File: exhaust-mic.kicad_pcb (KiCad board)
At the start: 4 copper layers, 72 x 55 mm, 131 parts, among them J1 XH-6pol_Power_CAN, J2 XH-5pol_MicA, J3 XH-5pol_MicB, J4 USB-C, J5 microSD_PushPush, J6 GPS_unbestueckt, J7 I2C_Erweiterung, Q1 ZXMP6A17E6, Q3 2N7002, Q4 2N7002, SW1 RESET, SW2 BOOT, SW3 REC, SW4 MARK, U1 LM5164DDA, U2 TLV1117LV33, U3 TPS7A2033, U5 PCM1863DBT, U6 ESP32-S3-WROOM-1-N8R2, U7 DS3231SN, U8 SN65HVD230D, Y1 24.576MHz

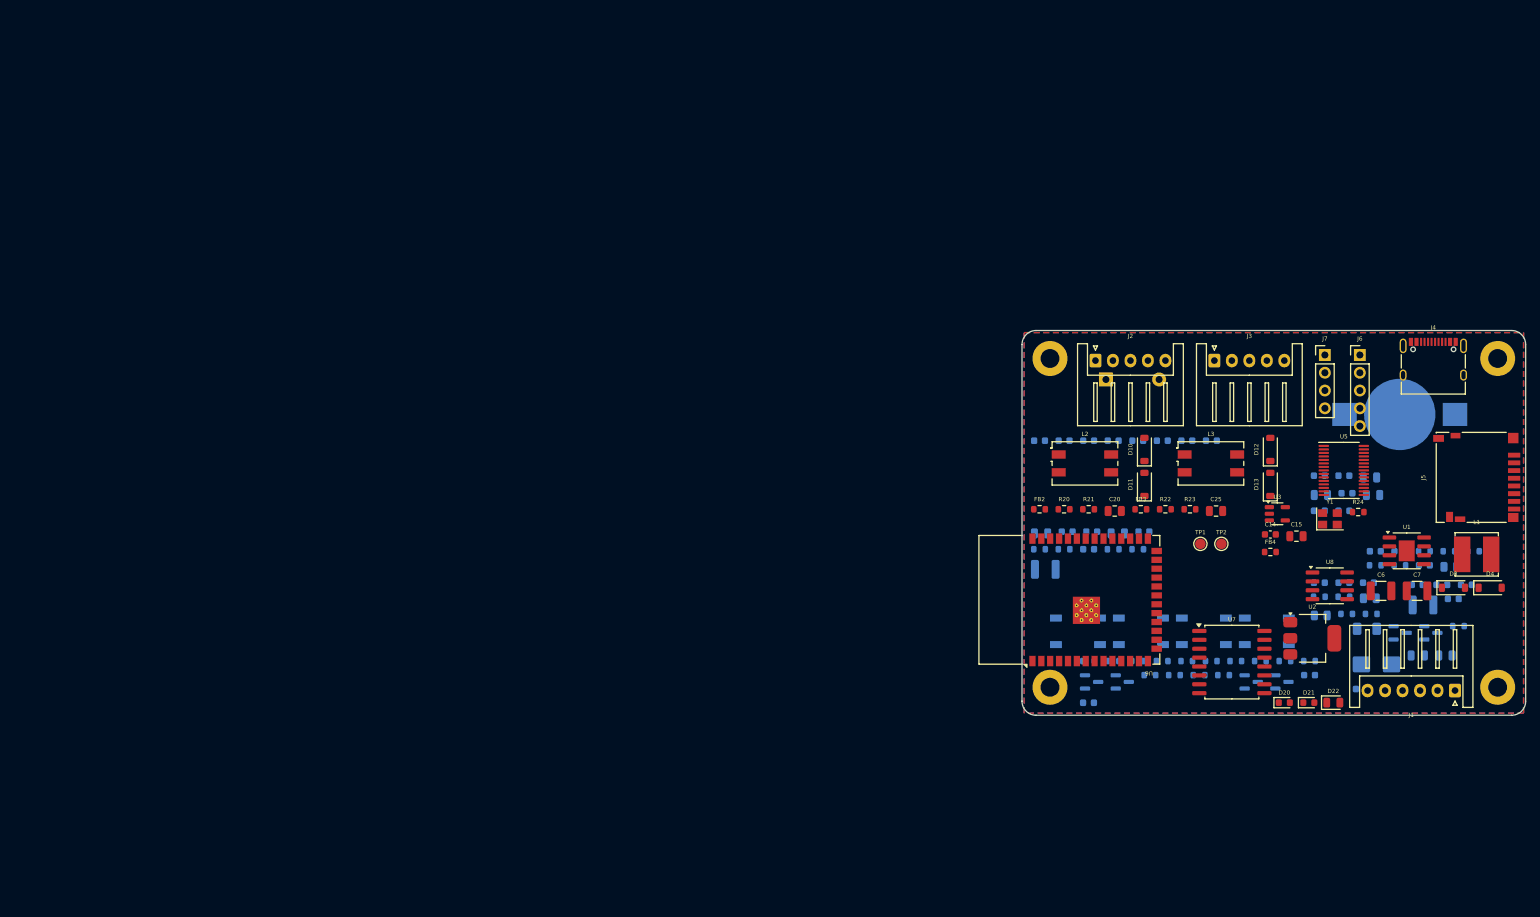
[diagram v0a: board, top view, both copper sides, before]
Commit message: Layout verdrahten, ERC/DRC bereinigen, Werkzeugkette auf KiCad 10
Mikrofonkopf ist fertig verdrahtet (0 offene Verbindungen, 0 DRC-Fehler).
Auf der Hauptplatine bleiben 16 Verbindungen offen, ebenfalls ohne
DRC-Fehler; sie sind im interaktiven Router von KiCad zu schliessen.

Schaltplan
- 3 Speisepin-Fehler behoben (+4V6, ADC-AVDD, Uhrenbatterie brauchen ein
  Speiseflag - sie werden ueber Drossel, Ferrit bzw. Zelle gespeist und
  haben damit keine Quelle im Sinne der Regelpruefung)
- Netzname GND_CHASSIS entfernt: lag auf demselben Knoten wie GND
- TLV1117LV33 hatte einen Pin 4 fuer die Kuehlfahne, den es im Footprint
  SOT-223-3_TabPin2 nicht gibt - dort traegt Pad 2 die Fahne
- Piezo von Durchsteck- auf SMD-Ausfuehrung (Murata PKMCS0909E): fuer den
  12,5-mm-Typ gibt es keine Position, an der seine Anschluesse nicht auf
  der Gegenseite auf Pads treffen
- ERC laeuft jetzt fehlerfrei

Layout
- Durchsteckpads belegen beide Seiten. J1, J4 und J6 standen ueber
  rueckseitigen Bauteilen; das waren vier echte Kurzschluesse, unter
  anderem GPS_PPS gegen Masse an der Knopfzelle. Die eigene Pruefung
  vergleicht Durchsteckpads jetzt gegen beide Seiten, pad-genau
- In2 traegt keine Versorgungsinseln mehr, sondern Signale. Vorher wich
  der Autorouter auf die Masseflaeche aus - 140 Segmente aus 30 Netzen
  quer durch In1. Der DSN-Export kennzeichnet In1 nun als Versorgungslage
- Masseflaechen auf den Aussenlagen mit Naehvias an In1 angebunden und auf
  automatische Inselentfernung gestellt
- Netzklasse auf 0,18 mm Bahn, 0,15 mm Abstand, 0,5/0,25-mm-Via verengt;
  mit KiCads Vorgabewerten blieb rund ein Dutzend Verbindungen mehr offen
- Beschaffungsfelder unsichtbar und auf die Fab-Lage: sichtbar im
  Siebdruck ueberdecken die Herstellernummern die halbe Platine, das
  waren 151 der urspruenglich 214 Regelwarnungen

Werkzeuge
- pipeline.sh fasst den Layoutlauf zusammen
- fix_drc.py nimmt KiCads Regelpruefung als Instanz und entfernt, was sie
  beanstandet - die eigenen Abst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
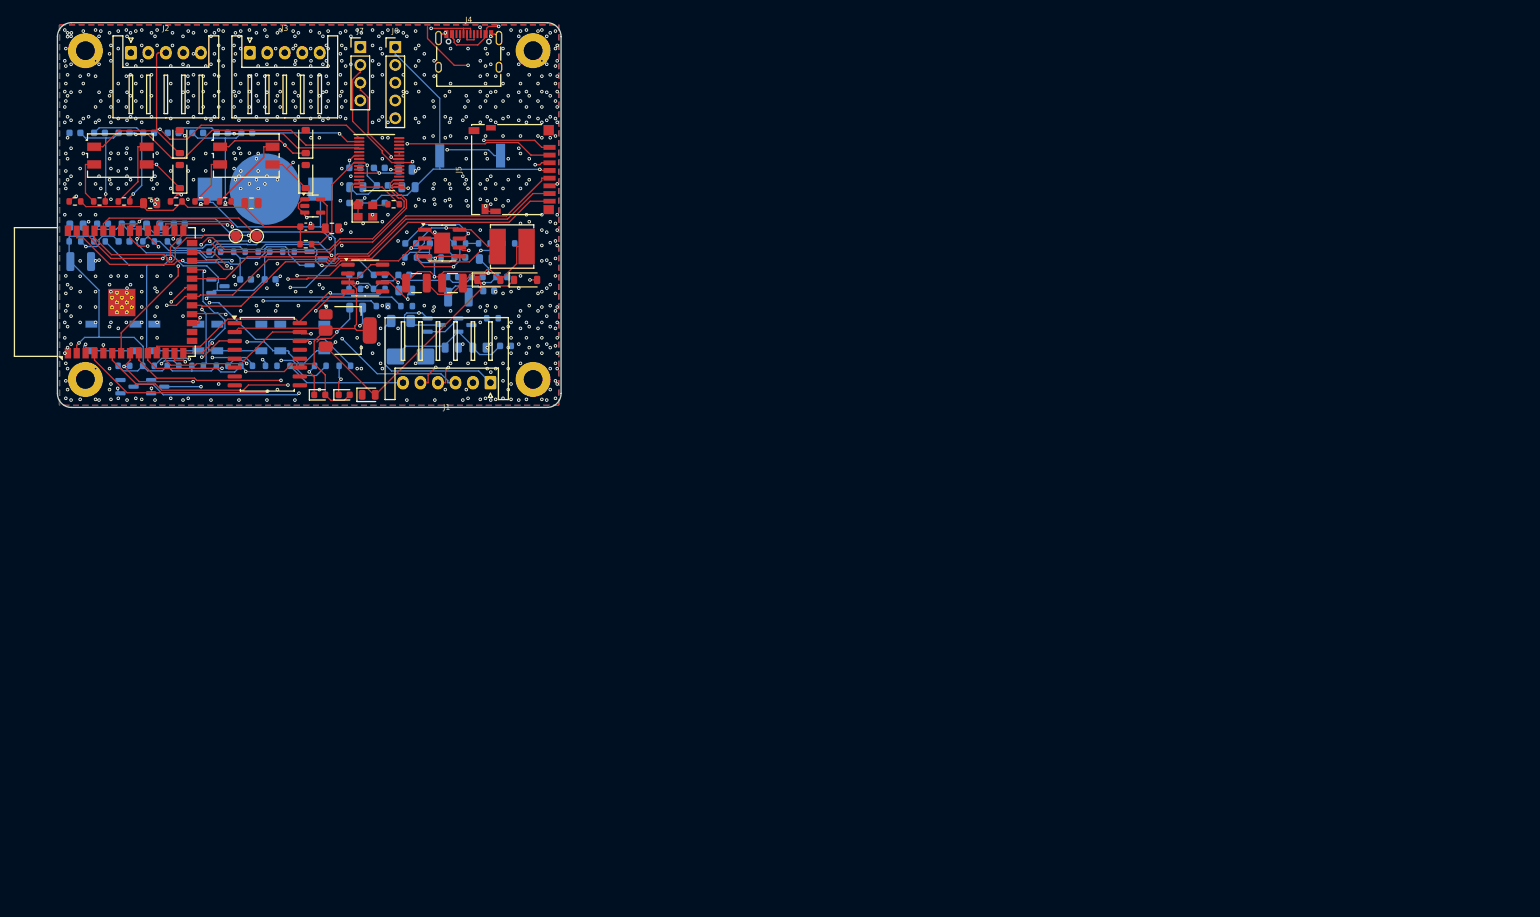
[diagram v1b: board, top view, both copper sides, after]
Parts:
- BT1: footprint BatteryHolder_Keystone_3000_1x12mm -> Battery:BatteryHolder_Keystone_3000_1x12mm
- C1, C15, C2, C20, C25, C32, C33, C35, C41, C45: footprint C_0805_2012Metric -> Capacitor_SMD:C_0805_2012Metric
- C10, C12, C13, C14, C16, C17, C21, C22, C23, C24, C26, C27, C28, C29, C3, C30, C31, C34, C36, C37, C4, C42, C43, C44, C46, C5, C50, C51, C52, C8, C9: footprint C_0603_1608Metric -> Capacitor_SMD:C_0603_1608Metric
- C11, C40, C6, C7: footprint C_1210_3225Metric -> Capacitor_SMD:C_1210_3225Metric
- D1, D5, D6, Q1, Q3, Q4: footprint SOT-23 -> Package_TO_SOT_SMD:SOT-23
- D10, D11, D12, D13, D3, D4: footprint D_SOD-123 -> Diode_SMD:D_SOD-123
- D2: footprint D_SMB -> Diode_SMD:D_SMB
- D20, D21: footprint LED_0603_1608Metric -> LED_SMD:LED_0603_1608Metric
- D22: footprint LED_0805_2012Metric -> LED_SMD:LED_0805_2012Metric
- F1: footprint Fuse_1206_3216Metric -> Fuse:Fuse_1206_3216Metric
- FB2, FB3, FB4, R1, R10, R11, R12, R2, R20, R21, R22, R23, R24, R3, R30, R31, R34, R35, R4, R40, R41, R42, R43, R44, R45, R46, R47, R48, R5, R50, R51, R52, R54, R55, R6, R9: footprint R_0603_1608Metric -> Resistor_SMD:R_0603_1608Metric
- J1: footprint JST_XH_S6B-XH-A_1x06_P2.50mm_Horizontal -> Connector_JST:JST_XH_S6B-XH-A_1x06_P2.50mm_Horizontal
- J2, J3: footprint JST_XH_S5B-XH-A_1x05_P2.50mm_Horizontal -> Connector_JST:JST_XH_S5B-XH-A_1x05_P2.50mm_Horizontal
- J4: footprint USB_C_Receptacle_XKB_U262-16XN-4BVC11 -> Connector_USB:USB_C_Receptacle_XKB_U262-16XN-4BVC11
- J5: footprint microSD_HC_Hirose_DM3D-SF -> Connector_Card:microSD_HC_Hirose_DM3D-SF
- J6: footprint PinHeader_1x05_P2.54mm_Vertical -> Connector_PinHeader_2.54mm:PinHeader_1x05_P2.54mm_Vertical
- J7: footprint PinHeader_1x04_P2.54mm_Vertical -> Connector_PinHeader_2.54mm:PinHeader_1x04_P2.54mm_Vertical
- L1: footprint L_Bourns_SRN6045TA -> Inductor_SMD:L_Bourns_SRN6045TA
- L2, L3: footprint L_CommonMode_Wuerth_WE-SL2 -> Inductor_SMD:L_CommonMode_Wuerth_WE-SL2
- LS1: value Piezo -> Piezo_SMD; footprint Buzzer_12x9.5RM7.6 -> Buzzer_Beeper:Buzzer_Murata_PKMCS0909E
- R49, R53, R7: footprint R_0805_2012Metric -> Resistor_SMD:R_0805_2012Metric
- SW1, SW2, SW3, SW4: footprint SW_SPST_TL3342 -> Button_Switch_SMD:SW_SPST_TL3342
- TP1, TP2: footprint TestPoint_Pad_D1.5mm -> TestPoint:TestPoint_Pad_D1.5mm
- U1: footprint SOIC-8-1EP_3.9x4.9mm_P1.27mm_EP2.29x3mm -> Package_SO:SOIC-8-1EP_3.9x4.9mm_P1.27mm_EP2.29x3mm
- U2: footprint SOT-223-3_TabPin2 -> Package_TO_SOT_SMD:SOT-223-3_TabPin2
- U3: footprint SOT-23-5 -> Package_TO_SOT_SMD:SOT-23-5
- U5: footprint TSSOP-30_4.4x7.8mm_P0.5mm -> exhaust-mic:TSSOP-30_4.4x7.8mm_P0.5mm
- U6: footprint ESP32-S3-WROOM-1 -> RF_Module:ESP32-S3-WROOM-1
- U7: footprint SOIC-16W_7.5x10.3mm_P1.27mm -> Package_SO:SOIC-16W_7.5x10.3mm_P1.27mm
- U8: footprint SOIC-8_3.9x4.9mm_P1.27mm -> Package_SO:SOIC-8_3.9x4.9mm_P1.27mm
- Y1: footprint Oscillator_SMD_Abracon_ASE-4Pin_3.2x2.5mm -> Oscillator:Oscillator_SMD_Abracon_ASE-4Pin_3.2x2.5mm
- moved BT1 165.4 mm to (29.7, 23.8)
- moved C16 162.3 mm to (26.9, 36.7)
- moved D6 162.3 mm to (22.9, 37.7)
- moved R10 146.7 mm to (26.0, 32.8)
- moved D5 146.7 mm to (37.0, 33.7)
- moved R11 146.7 mm to (29.5, 32.8)
- moved R12 146.7 mm to (33.0, 32.8)
- moved R9 146.7 mm to (22.5, 32.8)
- moved D2 144.9 mm to (50.5, 47.7)
- moved C1 144.9 mm to (56.4, 46.5)
- moved C2 144.9 mm to (60.3, 46.5)
- moved F1 144.9 mm to (49.1, 42.6)
- moved Q1 144.9 mm to (53.9, 43.2)
- moved R1 144.9 mm to (62.2, 42.3)
- moved D1 144.9 mm to (58.2, 43.2)
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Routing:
- net +3V3D: track 0.00 -> 223.0 mm, vias 0 -> 5
- net SD_CMD: track 0.00 -> 101.9 mm, vias 0 -> 3
- net I2C_SDA: track 0.00 -> 87.4 mm, vias 0 -> 3
- net SD_D2: track 0.00 -> 80.7 mm, vias 0 -> 3
- net SD_D3: track 0.00 -> 79.7 mm, vias 0 -> 3
- net USB_DP: track 0.00 -> 78.0 mm, vias 0 -> 2
- net I2C_SCL: track 0.00 -> 76.8 mm, vias 0 -> 2
- net USB_DM: track 0.00 -> 76.0 mm, vias 0 -> 2
- net SD_D0: track 0.00 -> 73.1 mm, vias 0 -> 2
- net +4V6: track 0.00 -> 72.4 mm, vias 0 -> 3
- net VBAT12: track 0.00 -> 72.3 mm, vias 0 -> 3
- net Net-(LS1--): track 0.00 -> 71.5 mm, vias 0 -> 2
- net PGOOD: track 0.00 -> 68.4 mm, vias 0 -> 3
- net I2S_BCK: track 0.00 -> 66.7 mm, vias 0 -> 2
- net SD_D1: track 0.00 -> 66.5 mm, vias 0 -> 1
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- removed copper zone on In2.Cu, net +3V3A
- removed copper zone on In2.Cu, net +3V3D
- removed copper zone on In2.Cu, net GND

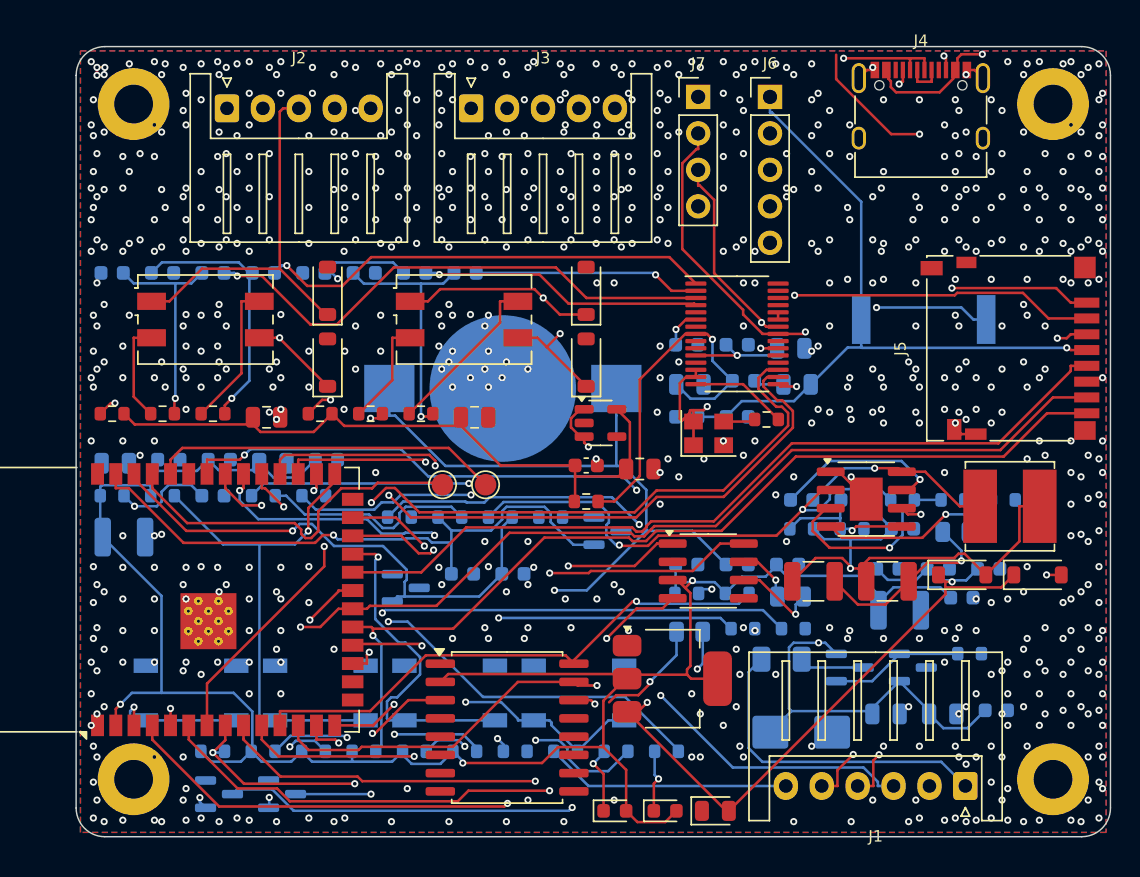
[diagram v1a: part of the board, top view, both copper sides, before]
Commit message: Freistellung der Kupferflaechen auf 0,15 mm: 16 -> 7 offene Verbindungen
Mit 0,25 mm Freistellung zerfielen die Masseflaechen an jeder Leiterbahn in
Inseln. Bei 0,15 mm - dem Wert der Netzklasse - quetscht sich das Kupfer
zwischen die Bahnen und bleibt zusammenhaengend. Zusammen mit einem
weiteren Routinglauf und Naehvias sinken die offenen Verbindungen auf der
Hauptplatine von 16 auf 7, weiterhin ohne DRC-Fehler.

Mindestbreite der Fuellung entsprechend auf 0,13 mm.
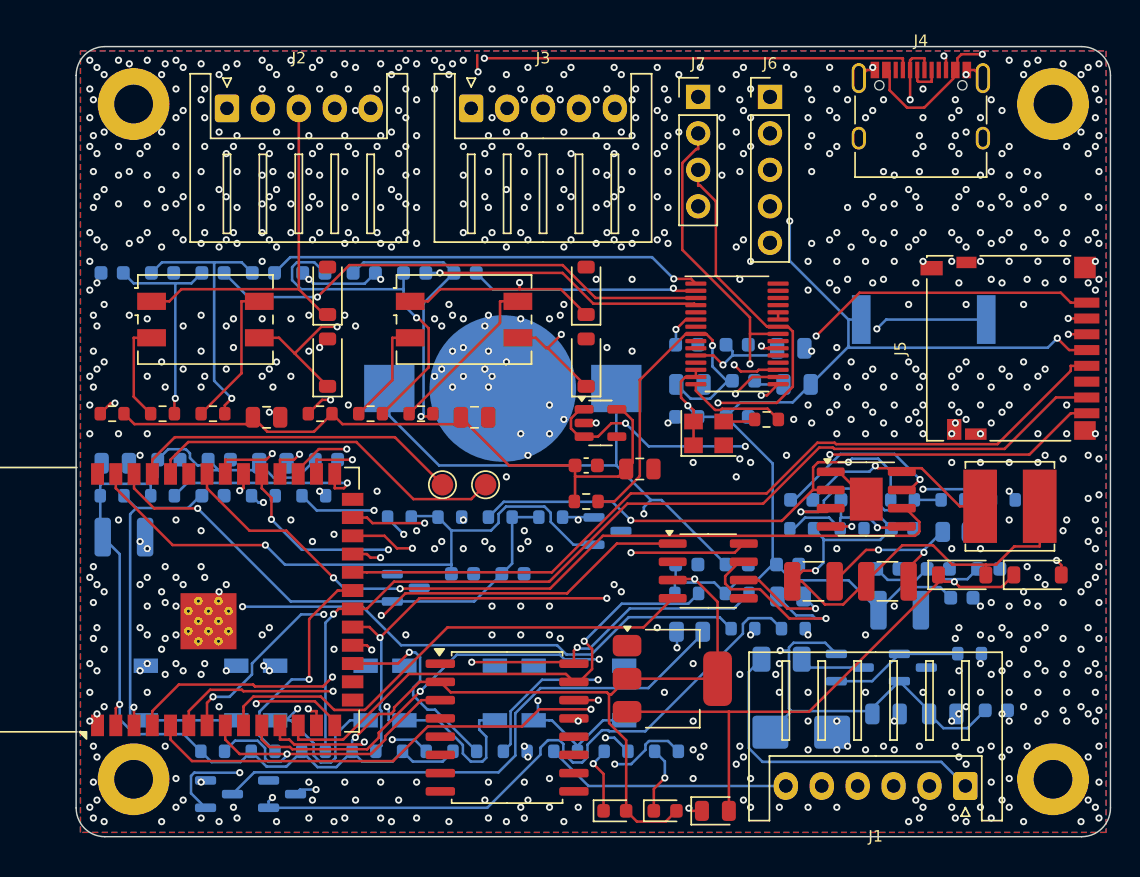
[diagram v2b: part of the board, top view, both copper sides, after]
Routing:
- net SD_CMD: track 101.9 -> 84.4 mm, vias 3 -> 2
- net USB_DP: track 78.0 -> 61.4 mm
- net SD_D3: track 79.7 -> 94.2 mm, vias 3 -> 2
- net BUZZ: track 61.5 -> 74.2 mm, vias 3 -> 2
- net GND: track 29.7 -> 18.2 mm, vias 744 -> 822
- net PGOOD: track 68.4 -> 57.4 mm, vias 3 -> 2
- net +3V3D: track 223.0 -> 213.2 mm, vias 5 -> 6
- net Net-(J4-CC1): track 59.5 -> 68.6 mm
- net I2C_SCL: track 76.8 -> 85.7 mm, vias 2 -> 4
- net +4V6: track 72.4 -> 80.8 mm
- net CAN_TX: track 53.9 -> 46.4 mm
- net Net-(U6-IO0): track 35.5 -> 42.9 mm, vias 1 -> 2
- net I2C_SDA: track 87.4 -> 80.2 mm, vias 3 -> 2
- net I2S_LRCK: track 66.1 -> 59.2 mm
- net I2S_DOUT: track 59.2 -> 52.8 mm, vias 2 -> 3
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
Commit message: modified:   01-power.kicad_sch 	modified:   02-analog.kicad_sch 	modified:   03-adc.kicad_sch 	modified:   04-mcu.kicad_sch 	modified:   05-io.kicad_sch 	modified:   exhaust-mic.kicad_pcb 	modified:   exhaust-mic.kicad_pro 	modified:   exhaust-mic.kicad_sch 	modified:   mic-head/mic-head.kicad_pcb 	modified:   mic-head/mic-head.kicad_pro 	modified:   mic-head/mic-head.kicad_sch 	new file:   ~exhaust-mic.kicad_pro.lck
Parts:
- moved C1 136.4 mm to (173.4, 116.5)
- moved C12 136.4 mm to (178.7, 108.4)
- moved C14 136.4 mm to (152.6, 99.2)
- moved C20 136.4 mm to (130.3, 95.9)
- moved C21 136.4 mm to (119.6, 85.8)
- moved C23 136.4 mm to (126.6, 85.8)
- moved C24 136.4 mm to (130.1, 85.8)
- moved C28 136.4 mm to (140.6, 85.8)
- moved C29 136.4 mm to (144.1, 85.8)
- moved C30 136.4 mm to (159.6, 90.8)
- moved C33 136.4 mm to (159.8, 93.6)
- moved C35 136.4 mm to (167.2, 93.6)
- moved C36 136.4 mm to (159.6, 95.8)
- moved C4 136.4 mm to (167.6, 101.6)
- moved C41 136.4 mm to (119.8, 99.1)
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
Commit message: Werte der Ersatztypen nachziehen und Felder auf die Platine uebertragen
Vier Bauteile trugen nach dem Ersatz einen Wert, der nicht mehr zum
eingebauten Typ passte: U2 (NCP1117ST33), U3 (LP5907MFX-3.3), U8
(SN65HVD230Q) und Q1 (SI2309CDS). Die uebrigen fuenf Ersatztypen behalten
ihren Wert - LM5164DDA, 24.576MHz, BZX84C15, PMEG3020 und OPA2325 sind
Typbezeichnungen, die auch fuer die Ersatznummer gelten.

Die Beschaffungsfelder standen bisher nur im Schaltplan. KiCads Abgleich
vergleicht auch Felder und meldete darum fuer fast jedes Bauteil eine
Abweichung - 144 statt vorher 8. tools/sync_pcb_fields.py traegt Wert und
Felder aus der Netzliste in die Bauteile auf der Platine nach, unsichtbar
und auf der Fabrikationslage. Danach bleiben 18 Abweichungen auf der
Hauptplatine und 2 auf dem Mikrofonkopf, alle aelteren Datums: der
Schaltplan auf der Platte kennt Footprints, die so nicht baubar sind
(Superseal auf der Platine, TSSOP-30 mit falschem Raster, ESP32-S2-Modul),
das Layout hat sie laengst ersetzt.

Nebenbei zwei Fehler in der eigenen Pruefung behoben, die erst jetzt
auffielen: der Kantenabstand wurde gegen den Ursprung gerechnet, obwohl
KiCad die Kontur beim Bearbeiten auf die Blattmitte geschoben hat
(117/70 statt 0/0) - das ergab 2914 Scheinbeanstandungen. Und
PCB_VIA::GetWidth() will in KiCad 10 die Lage wissen.

DRC unveraendert: 0 Fehler, 10 Warnungen, 7 offene Verbindungen.
Stuecklisten, Fertigungsdaten und Schaltplan-PDFs neu erzeugt.
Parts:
- BT1: value CR1220 -> CR2032
- J1: value XH-6pol_Power_CAN -> Superseal_1.0_6pol
- J2: value XH-5pol_MicA -> Superseal_1.0_5pol_MicA
- J3: value XH-5pol_MicB -> Superseal_1.0_5pol_MicB
- LS1: value Piezo_SMD -> Piezo
- Q1: value ZXMP6A17E6 -> SI2309CDS
- U2: value TLV1117LV33 -> NCP1117ST33
- U3: value TPS7A2033 -> LP5907MFX-3.3
- U8: value SN65HVD230D -> SN65HVD230Q

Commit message: Footprints im Schaltplan auf den Stand des Layouts ziehen
Neun Bauteile trugen im Schaltplan einen Footprint, der so nicht baubar ist.
Das Layout hatte sie laengst ersetzt; jetzt steht es auch im Schaltplan:

  U5      TSSOP-30 4,4 x 9,7 / 0,65  ->  4,4 x 7,8 / 0,5  (Datenblatt)
  U6      ESP32-S2-WROOM             ->  ESP32-S3-WROOM-1
  L2, L3  L_CommonModeChoke_WE-SL2   ->  L_CommonMode_WE-SL2
  J1..J3  TE Superseal 1.0           ->  JST XH liegend
  BT1     Keystone 3034 / CR2032     ->  Keystone 3000 / CR1220
  LS1     Piezo bedrahtet 12 mm      ->  Murata-Landmuster 9 x 9 mm SMD

Wo sich damit das Bauteil aendert, sind Wert und Bestellnummer mitgezogen.
Zwei Punkte dabei zum Nachlesen:

* BT1 hat mit CR1220 rund ein Viertel der Kapazitaet von CR2032. Die
  Platine ist fuer den 12-mm-Halter gebohrt, darum folgt der Schaltplan.
* Der im Layout benannte Murata PKMCS0909E ist abgekuendigt ("Last Time
  Buy") und nur fuer 1,5 V spezifiziert, angesteuert wird aber mit 3,3 V.
  Bestellt wird darum ein 3-V-Typ gleicher Bauform (Same Sky
  CPT-9019A-SMT-TR); das Landmuster gehoert gegen das Datenblatt geprueft.

Damit sind die Steckverbinder J1..J3 beschaffbar - Superseal 1.0 gibt es bei
DigiKey nur kabelseitig. Offen bleiben noch J4 und MK1.

Schaltplanparitaet: 18 -> 9 Abweichungen auf der Hauptplatine, 2 auf dem
Mikrofonkopf. Die restlichen sind keine Footprints mehr, sondern Symbole:
U2 hat einen Pin 4, den das SOT-223 nicht hat, und dem microSD-Symbol fehlt
der Schirmanschluss. Beides steht im README.

Die Stueckliste fuehrt jetzt eine Spalte Hinweis - dort landen die
Ersatzgruende, die vorher nur im Schaltplan standen.

DRC unveraendert: 0 Fehler, 10 Warnungen, 7 offene Verbindungen. ERC
unveraendert. Stuecklisten, Fertigungsdaten und PDFs neu erzeugt.
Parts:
- BT1: value CR2032 -> CR1220
- J1: value Superseal_1.0_6pol -> JST_XH_6pol
- J2: value Superseal_1.0_5pol_MicA -> JST_XH_5pol_MicA
- J3: value Superseal_1.0_5pol_MicB -> JST_XH_5pol_MicB
- LS1: value Piezo -> Piezo_9x9_SMD
